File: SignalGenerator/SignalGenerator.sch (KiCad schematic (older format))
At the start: 25 parts

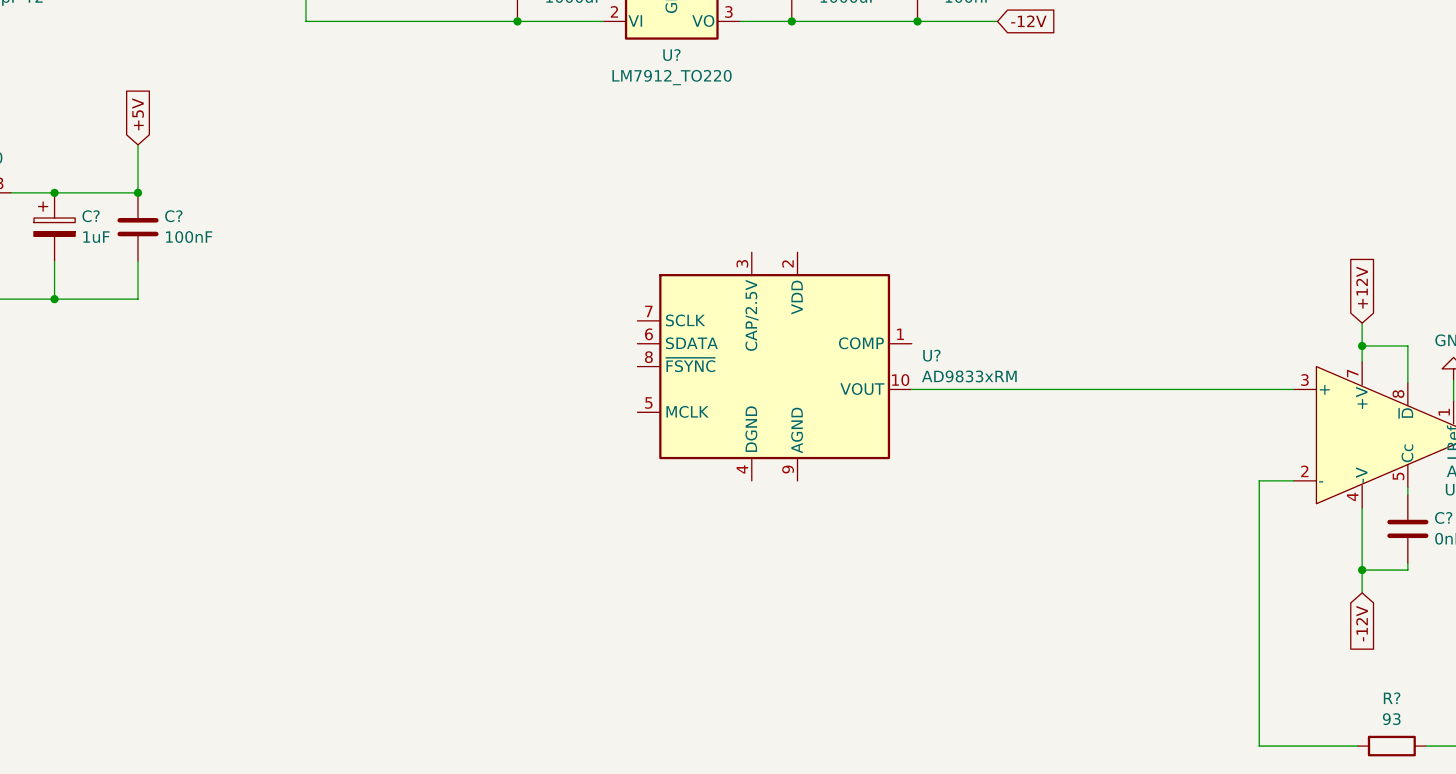
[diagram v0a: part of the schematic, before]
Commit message: Added DC offset to schematic
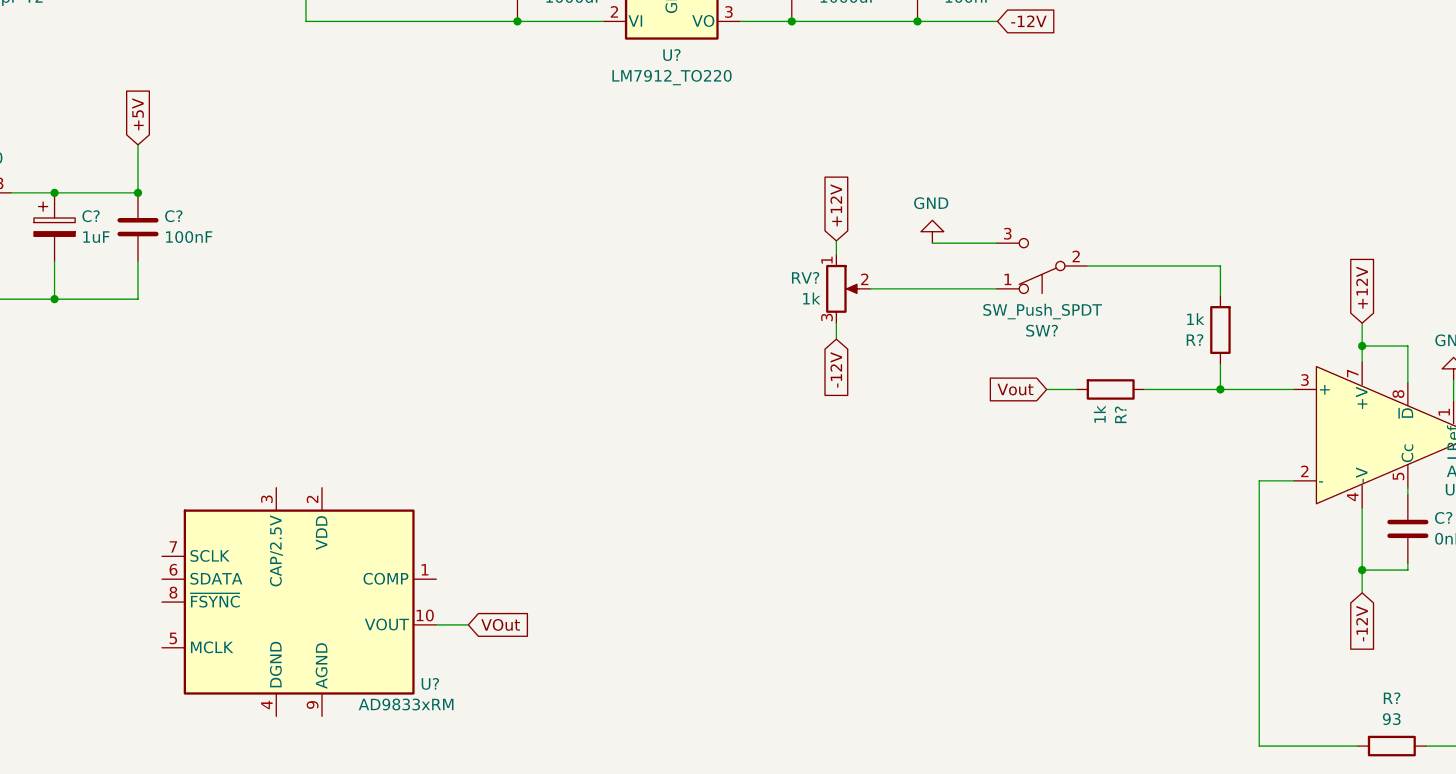
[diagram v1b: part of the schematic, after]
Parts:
- added R? (x2): 1k, symbol Device:R
- added RV?: 1k, symbol Device:R_POT
- added SW?: SW_Push_SPDT, symbol Switch:SW_Push_SPDT
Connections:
- net +12V: now also RV?.1
- net -12V: now also RV?.3
- net GND: now also SW?.3 (C)
- net at U?.3 (+): now also R?.1, R?.1; no longer U?.10 (VOUT)
- new net: RV?.2, SW?.1 (A)
- new net: R?.2, SW?.2 (B)
- new net VOut: U?.10 (VOUT)
- new net Vout: R?.2
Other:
- moved on the sheet: U?
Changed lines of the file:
@@
 L Interface:AD9833xRM U?
 U 1 1 6131BF32
-P 5350 3360
-F 0 "U?" H 5994 3406 50  0000 L CNN
-F 1 "AD9833xRM" H 5994 3315 50  0000 L CNN
-F 2 "Package_SO:MSOP-10_3x3mm_P0.5mm" H 5350 2760 50  0001 C CNN
-F 3 "https://www.analog.com/media/en/technical-documentation/data-sheets/ad9833.pdf" H 5300 3660 50  0001 C CNN
-	1    5350 3360
+P 3270 4390
+F 0 "U?" H 3800 4030 50  0000 L CNN
+F 1 "AD9833xRM" H 3530 3940 50  0000 L CNN
+F 2 "Package_SO:MSOP-10_3x3mm_P0.5mm" H 3270 3790 50  0001 C CNN
+F 3 "https://www.analog.com/media/en/technical-documentation/data-sheets/ad9833.pdf" H 3220 4690 50  0001 C CNN
+	1    3270 4390
 	1    0    0    -1
 $EndComp
@@
 Wire Wire Line
 	8320 3420 8320 3510
-Wire Wire Line
-	7620 3460 5950 3460
 $Comp
 L Connector:Conn_Coaxial J?
@@
 Text Notes 8490 4770 0    50   ~ 0
 G=1k/93+1
+$Comp
+L Switch:SW_Push_SPDT SW?
+U 1 1 618B491B
+P 6520 2920
+F 0 "SW?" H 6520 3205 50  0000 C CNN
+F 1 "SW_Push_SPDT" H 6520 3114 50  0000 C CNN
+F 2 "" H 6520 2920 50  0001 C CNN
+F 3 "~" H 6520 2920 50  0001 C CNN
+	1    6520 2920
+	-1   0    0    1
+$EndComp
+Text GLabel 5620 2810 1    50   Input ~ 0
++12V
+$Comp
+L Device:R_POT RV?
+U 1 1 618DC911
+P 5620 3020
+F 0 "RV?" H 5550 3066 50  0000 R CNN
+F 1 "1k" H 5550 2975 50  0000 R CNN
+F 2 "" H 5620 3020 50  0001 C CNN
+F 3 "~" H 5620 3020 50  0001 C CNN
+	1    5620 3020
+	1    0    0    -1
+$EndComp
+Wire Wire Line
+	5620 2810 5620 2870
+Text GLabel 5620 3240 3    50   Input ~ 0
+-12V
+Wire Wire Line
+	5620 3170 5620 3240
+Wire Wire Line
+	5770 3020 6320 3020
+$Comp
+L power:GND #PWR?
+U 1 1 618FD81E
+P 6040 2820
+F 0 "#PWR?" H 6040 2570 50  0001 C CNN
+F 1 "GND" H 6045 2647 50  0000 C CNN
+F 2 "" H 6040 2820 50  0001 C CNN
+F 3 "" H 6040 2820 50  0001 C CNN
+	1    6040 2820
+	-1   0    0    1
+$EndComp
+Wire Wire Line
+	6320 2820 6040 2820
+Text GLabel 4010 4490 2    50   Input ~ 0
+VOut
+Wire Wire Line
+	3870 4490 4010 4490
+Text GLabel 6540 3460 0    50   Input ~ 0
+Vout
+$Comp
+L Device:R R?
+U 1 1 619165E3
+P 6820 3460
+F 0 "R?" H 6890 3506 50  0000 L CNN
+F 1 "1k" H 6890 3415 50  0000 L CNN
+F 2 "" V 6750 3460 50  0001 C CNN
+F 3 "~" H 6820 3460 50  0001 C CNN
+	1    6820 3460
+	0    1    1    0
+$EndComp
+Wire Wire Line
+	6540 3460 6670 3460
+Wire Wire Line
+	6970 3460 7300 3460
+$Comp
+L Device:R R?
+U 1 1 6191B2D4
+P 7300 3200
+F 0 "R?" H 7370 3246 50  0000 L CNN
+F 1 "1k" H 7370 3155 50  0000 L CNN
+F 2 "" V 7230 3200 50  0001 C CNN
+F 3 "~" H 7300 3200 50  0001 C CNN
+	1    7300 3200
+	-1   0    0    1
+$EndComp
+Wire Wire Line
+	7300 3350 7300 3460
+Connection ~ 7300 3460
+Wire Wire Line
+	7300 3460 7620 3460
+Wire Wire Line
+	6720 2920 7300 2920
+Wire Wire Line
+	7300 2920 7300 3050
 $EndSCHEMATC

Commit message: doing some small stuff
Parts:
- removed R?: 1k, symbol Device:R
- removed R?: 93, symbol Device:R
- added C? (x2): 100nF, symbol Device:C
- added R?: 1k, symbol Device:R
- added RV?: 50k, symbol Device:R_POT
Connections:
- net +12V: now also C?.2
- net -12V: now also C?.1
- net GND: now also U?.4 (DGND), U?.9 (AGND), C?.1, C?.2
- net at U?.2 (-): now also R?.2
- net at J?.1 (In), U?.6: now also RV?.2, RV?.3
- new net: R?.1, RV?.1
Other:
- note added: "Spit/star ground for digital and analog"
- note removed: "G=1k/93+1"
- moved on the sheet: U?
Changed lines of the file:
@@
 L Interface:AD9833xRM U?
 U 1 1 6131BF32
-P 3270 4390
-F 0 "U?" H 3800 4030 50  0000 L CNN
-F 1 "AD9833xRM" H 3530 3940 50  0000 L CNN
-F 2 "Package_SO:MSOP-10_3x3mm_P0.5mm" H 3270 3790 50  0001 C CNN
-F 3 "https://www.analog.com/media/en/technical-documentation/data-sheets/ad9833.pdf" H 3220 4690 50  0001 C CNN
-	1    3270 4390
+P 3250 4690
+F 0 "U?" H 3780 4330 50  0000 L CNN
+F 1 "AD9833xRM" H 3510 4240 50  0000 L CNN
+F 2 "Package_SO:MSOP-10_3x3mm_P0.5mm" H 3250 4090 50  0001 C CNN
+F 3 "https://www.analog.com/media/en/technical-documentation/data-sheets/ad9833.pdf" H 3200 4990 50  0001 C CNN
+	1    3250 4690
 	1    0    0    -1
 $EndComp
@@
 	-1   0    0    1
 $EndComp
-Text GLabel 7920 3170 1    50   Input ~ 0
+Text GLabel 7920 2970 1    50   Input ~ 0
 +12V
 Text GLabel 7920 4350 3    50   Input ~ 0
@@
 $EndComp
 Wire Wire Line
-	7920 3170 7920 3270
+	7920 2970 7920 3100
 Wire Wire Line
 	8120 3890 8120 3920
 Wire Wire Line
-	7920 3980 7920 4250
+	7920 3980 7920 4140
 Wire Wire Line
 	8120 4220 8120 4250
@@
 	1    0    0    -1
 $EndComp
-Wire Wire Line
-	8520 3660 9000 3660
 $Comp
 L power:GND #PWR?
@@
 Wire Wire Line
 	9760 3860 9760 3970
-$Comp
-L Device:R R?
-U 1 1 617B2257
-P 9000 4150
-F 0 "R?" H 9070 4196 50  0000 L CNN
-F 1 "1k" H 9070 4105 50  0000 L CNN
-F 2 "" V 8930 4150 50  0001 C CNN
-F 3 "~" H 9000 4150 50  0001 C CNN
-	1    9000 4150
-	1    0    0    -1
-$EndComp
-Wire Wire Line
-	9000 4000 9000 3660
-Connection ~ 9000 3660
-Wire Wire Line
-	9000 3660 9560 3660
-$Comp
-L Device:R R?
-U 1 1 617B4754
-P 8050 5020
-F 0 "R?" V 7843 5020 50  0000 C CNN
-F 1 "93" V 7934 5020 50  0000 C CNN
-F 2 "" V 7980 5020 50  0001 C CNN
-F 3 "~" H 8050 5020 50  0001 C CNN
-	1    8050 5020
-	0    1    1    0
-$EndComp
-Wire Wire Line
-	9000 4300 9000 5020
-Wire Wire Line
-	9000 5020 8200 5020
-Wire Wire Line
-	7620 3860 7470 3860
-Wire Wire Line
-	7470 3860 7470 5020
-Wire Wire Line
-	7470 5020 7900 5020
-Text Notes 8490 4770 0    50   ~ 0
-G=1k/93+1
 $Comp
 L Switch:SW_Push_SPDT SW?
@@
 Wire Wire Line
 	6320 2820 6040 2820
-Text GLabel 4010 4490 2    50   Input ~ 0
+Text GLabel 3990 4790 2    50   Input ~ 0
 VOut
 Wire Wire Line
-	3870 4490 4010 4490
+	3850 4790 3990 4790
 Text GLabel 6540 3460 0    50   Input ~ 0
 Vout
@@
 Wire Wire Line
 	7300 2920 7300 3050
+Wire Wire Line
+	8520 3660 9020 3660
+$Comp
+L Device:R R?
+U 1 1 618FD982
+P 7690 5060
+F 0 "R?" V 7483 5060 50  0000 C CNN
+F 1 "1k" V 7574 5060 50  0000 C CNN
+F 2 "" V 7620 5060 50  0001 C CNN
+F 3 "~" H 7690 5060 50  0001 C CNN
+	1    7690 5060
+	0    1    1    0
+$EndComp
+$Comp
+L Device:R_POT RV?
+U 1 1 618FF066
+P 9020 4380
+F 0 "RV?" H 8950 4426 50  0000 R CNN
+F 1 "50k" H 8950 4335 50  0000 R CNN
+F 2 "" H 9020 4380 50  0001 C CNN
+F 3 "~" H 9020 4380 50  0001 C CNN
+	1    9020 4380
+	-1   0    0    1
+$EndComp
+Wire Wire Line
+	9020 4230 9020 4010
+Connection ~ 9020 3660
+Wire Wire Line
+	9020 3660 9560 3660
+Wire Wire Line
+	9020 4530 9020 5060
+Wire Wire Line
+	9020 5060 7840 5060
+Wire Wire Line
+	8870 4380 8750 4380
+Wire Wire Line
+	8750 4380 8750 4010
+Wire Wire Line
+	8750 4010 9020 4010
+Connection ~ 9020 4010
+Wire Wire Line
+	9020 4010 9020 3660
+Wire Wire Line
+	7620 3860 7260 3860
+Wire Wire Line
+	7260 3860 7260 5060
+Wire Wire Line
+	7260 5060 7540 5060
+$Comp
+L Device:C C?
+U 1 1 6191899E
+P 7660 4140
+F 0 "C?" H 7775 4186 50  0000 L CNN
+F 1 "100nF" H 7775 4095 50  0000 L CNN
+F 2 "" H 7698 3990 50  0001 C CNN
+F 3 "~" H 7660 4140 50  0001 C CNN
+	1    7660 4140
+	0    1    1    0
+$EndComp
+$Comp
+L power:GND #PWR?
+U 1 1 61918FD4
+P 7390 4240
+F 0 "#PWR?" H 7390 3990 50  0001 C CNN
+F 1 "GND" H 7395 4067 50  0000 C CNN
+F 2 "" H 7390 4240 50  0001 C CNN
+F 3 "" H 7390 4240 50  0001 C CNN
+	1    7390 4240
+	1    0    0    -1
+$EndComp
+Wire Wire Line
+	7510 4140 7390 4140
+Wire Wire Line
+	7390 4140 7390 4240
+Wire Wire Line
+	7810 4140 7920 4140
+Connection ~ 7920 4140
+Wire Wire Line
+	7920 4140 7920 4250
+$Comp
+L Device:C C?
+U 1 1 61920E4D
+P 8640 3100
+F 0 "C?" H 8755 3146 50  0000 L CNN
+F 1 "100nF" H 8755 3055 50  0000 L CNN
+F 2 "" H 8678 2950 50  0001 C CNN
+F 3 "~" H 8640 3100 50  0001 C CNN
+	1    8640 3100
+	0    1    1    0
+$EndComp
+Wire Wire Line
+	8490 3100 7920 3100
+Connection ~ 7920 3100
+Wire Wire Line
+	7920 3100 7920 3270
+$Comp
+L power:GND #PWR?
+U 1 1 61923E3C
+P 8980 3220
+F 0 "#PWR?" H 8980 2970 50  0001 C CNN
+F 1 "GND" H 8985 3047 50  0000 C CNN
+F 2 "" H 8980 3220 50  0001 C CNN
+F 3 "" H 8980 3220 50  0001 C CNN
+	1    8980 3220
+	1    0    0    -1
+$EndComp
+Wire Wire Line
+	8790 3100 8980 3100
+Wire Wire Line
+	8980 3100 8980 3220
+$Comp
+L power:GND #PWR?
+U 1 1 6192AAD0
+P 3350 5400
+F 0 "#PWR?" H 3350 5150 50  0001 C CNN
+F 1 "GND" H 3355 5227 50  0000 C CNN
+F 2 "" H 3350 5400 50  0001 C CNN
+F 3 "" H 3350 5400 50  0001 C CNN
+	1    3350 5400
+	1    0    0    -1
+$EndComp
+$Comp
+L power:GND #PWR?
+U 1 1 6192BA48
+P 3150 5400
+F 0 "#PWR?" H 3150 5150 50  0001 C CNN
+F 1 "GND" H 3155 5227 50  0000 C CNN
+F 2 "" H 3150 5400 50  0001 C CNN
+F 3 "" H 3150 5400 50  0001 C CNN
+	1    3150 5400
+	1    0    0    -1
+$EndComp
+Wire Wire Line
+	3150 5190 3150 5400
+Wire Wire Line
+	3350 5190 3350 5400
+Text Notes 2560 5740 0    50   ~ 0
+Spit/star ground for digital and analog
 $EndSCHEMATC

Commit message: Made alot off changes. schematics is much closer to done
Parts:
- added C? (x4): 100nF, symbol Device:C
- added C?: 10uF, symbol Device:C
- added C?: 10uf, symbol Device:C
- added C? (x2): 22p, symbol Device:C
- added C?: 10nF, symbol Device:C
- added D?: LED, symbol Device:LED
- added J?: AVR-ICSP, symbol Connector_Generic:Conn_02x03_Odd_Even
- added J?: Buss PD, symbol Connector_Generic:Conn_02x05_Odd_Even
- added J?: I2C, symbol Connector_Generic:Conn_02x02_Odd_Even
- added R?: 50, symbol Device:R
- added R?: 10k, symbol Device:R
- added R?: 200, symbol Device:R
- added R? (x2): 4.7k, symbol Device:R
- added U?: ATmega328P-AU, Package_QFP:TQFP-32_7x7mm_P0.8mm, symbol MCU_Microchip_ATmega:ATmega328P-AU
- added X?: ECS-3951M-250-BN-TR, SignalGenerator:ECS-3951M-250-BN-TR, symbol Oscillator:ECS-2520MV-xxx-xx
- added Y?: 16MHz, symbol Device:Crystal
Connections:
- net +5V: now also U?.2 (VDD), C?.1, C?.1, C?.2, C?.2, C?.2, C?.2, J?.2 (Pin_2), J?.3 (Pin_3), J?.9 (Pin_9), R?.2, R?.2, R?.2, U?.18 (AVCC), U?.4 (VCC), U?.6 (VCC), X?.4 (VDD)
- net GND: now also C?.1, C?.1, C?.1, C?.2, C?.2, C?.2, C?.2, C?.2, J?.10 (Pin_10), J?.4 (Pin_4), J?.6 (Pin_6), R?.1, R?.2, U?.21 (GND), U?.3 (GND), U?.5 (GND), X?.2 (GND)
- net at U?.1 (COMP): now also C?.1
- net at U?.3 (CAP/2.5V): now also C?.1
- net at U?.5 (MCLK): now also X?.3 (OUT)
- net MOSI: now reaches U?.6 (SDATA)
- net MOSI: now also J?.4 (Pin_4), U?.15 (PB3)
- net SCLK: now reaches U?.7 (SCLK)
- net SCLK: now also J?.3 (Pin_3), U?.17 (PB5)
- net FSYNC: now reaches U?.8 (~FSYNC)
- net FSYNC: now also U?.14 (PB2)
- net at J?.1 (In), RV?.2, RV?.3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: now also R?.2
- new net: D?.2 (A), U?.12 (PB0)
- new net: D?.1 (K), R?.1
- new net MISO: J?.1 (Pin_1), U?.16 (PB4)
- new net PD0: J?.1 (Pin_1), U?.30 (PD0)
- new net PD1: J?.2 (Pin_2), U?.31 (PD1)
- new net PD2: J?.3 (Pin_3), U?.32 (PD2)
- new net PD3: J?.4 (Pin_4), U?.1 (PD3)
- new net PD4: J?.5 (Pin_5), U?.2 (PD4)
- new net PD5: J?.6 (Pin_6), U?.9 (PD5)
- new net PD6: J?.7 (Pin_7), U?.10 (PD6)
- new net PD7: J?.8 (Pin_8), U?.11 (PD7)
- new net RESET: J?.5 (Pin_5), R?.1, U?.29 (~RESET~/PC6)
- new net SCL: J?.2 (Pin_2), R?.1, U?.28 (PC5)
- new net SDA: J?.1 (Pin_1), R?.1, U?.27 (PC4)
- new net XTAL1: C?.1, U?.7 (XTAL1/PB6), Y?.1
- new net XTAL2: C?.1, U?.8 (XTAL2/PB7), Y?.2
- no-connect marks 0 -> 5
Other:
- note added: "Maybe not 10k"
- note added: "Spit/star ground for digital and analog?\nNope gonna try to use min of 20xdistance between analog and digital of the distance between top copper and groundplane beneath.\nLook at https://www.youtube.com/watch?v=vALt6Sd9vlY&t=2312s"
- note removed: "Spit/star ground for digital and analog"
- moved on the sheet: C?, J?, R?, RV?, SW?, U?
